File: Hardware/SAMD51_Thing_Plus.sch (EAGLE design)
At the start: 48 parts, among them J6 AMP FCI 10103594-0001LF, Q1 2.5A/30V, U1 MCP73831, U2 ATSAMD51J20A-A, U3 AP2112K-3.3V, U4 4MB Flash, Y1 32.768kHz

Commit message: Convert labels to Fredoka, headers to smaller square pads
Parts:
- J1: device SparkFun-Connectors:CONN_12NO_SILK -> SparkFun-Connectors:CONN_12SM_SQ_NO_SILK
- J2: device SparkFun-Connectors:CONN_161X16_NO_SILK -> SparkFun-Connectors:CONN_161X16_SM_SQ_NOSILK
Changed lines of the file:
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@@
 <part name="GND8" library="SparkFun-Aesthetics" deviceset="GND" device=""/>
 <part name="J6" library="SparkFun-Connectors" deviceset="USB_MICRO-B" device="_HALF_PTH" value="AMP FCI 10103594-0001LF"/>
-<part name="J1" library="SparkFun-Connectors" deviceset="CONN_12" device="NO_SILK"/>
-<part name="J2" library="SparkFun-Connectors" deviceset="CONN_16" device="1X16_NO_SILK"/>
+<part name="J1" library="SparkFun-Connectors" deviceset="CONN_12" device="SM_SQ_NO_SILK"/>
+<part name="J2" library="SparkFun-Connectors" deviceset="CONN_16" device="1X16_SM_SQ_NOSILK"/>
 <part name="GND5" library="SparkFun-Aesthetics" deviceset="GND" device=""/>
 <part name="GND7" library="SparkFun-Aesthetics" deviceset="GND" device=""/>

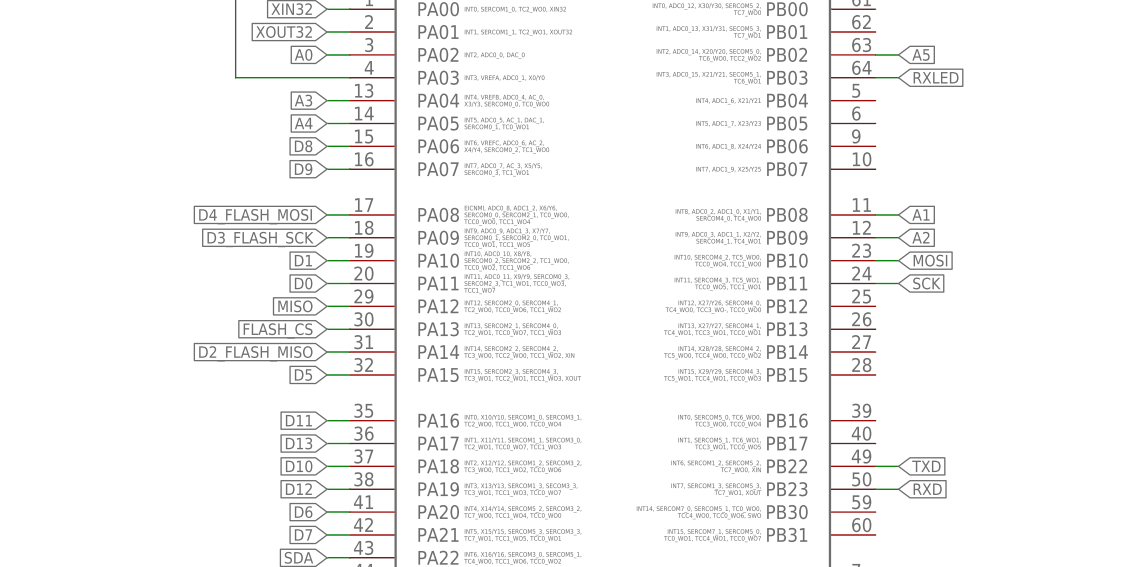
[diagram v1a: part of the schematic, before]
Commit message: Fix SPI pinout for flash and header
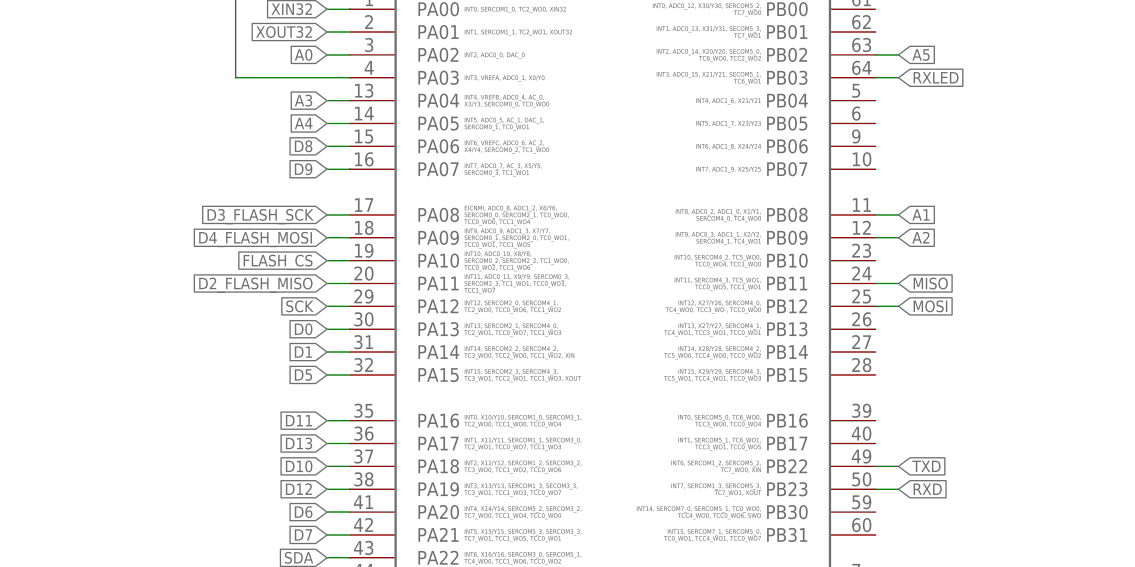
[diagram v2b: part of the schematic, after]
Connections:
- net D0: now also U2.PA13; no longer U2.PA11
- net D1: now also U2.PA14; no longer U2.PA10
- net D2_FLASH_MISO: now also U2.PA11; no longer U2.PA14
- net D3_FLASH_SCK: now also U2.PA08; no longer U2.PA09
- net D4_FLASH_MOSI: now also U2.PA09; no longer U2.PA08
- net FLASH_CS: now also U2.PA10; no longer U2.PA13
- net MISO: now also U2.PB11; no longer U2.PA12
- net MOSI: now also U2.PB12; no longer U2.PB10
- net SCK: now also U2.PA12; no longer U2.PB11
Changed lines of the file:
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@@
 <net name="D3_FLASH_SCK" class="0">
-<segment>
-<pinref part="U2" gate="G$1" pin="PA09"/>
-<wire x1="93.98" y1="121.92" x2="91.44" y2="121.92" width="0.1524" layer="91"/>
-<label x="91.44" y="121.92" size="1.27" layer="95" font="vector" rot="R180" xref="yes"/>
-</segment>
 <segment>
 <pinref part="U4" gate="G$1" pin="SCK"/>
@@
 <label x="396.24" y="152.4" size="1.27" layer="95" xref="yes"/>
 </segment>
+<segment>
+<pinref part="U2" gate="G$1" pin="PA08"/>
+<wire x1="93.98" y1="124.46" x2="91.44" y2="124.46" width="0.1524" layer="91"/>
+<label x="91.44" y="124.46" size="1.27" layer="95" rot="R180" xref="yes"/>
+</segment>
 </net>
 <net name="D2_FLASH_MISO" class="0">
-<segment>
-<pinref part="U2" gate="G$1" pin="PA14"/>
-<wire x1="93.98" y1="109.22" x2="91.44" y2="109.22" width="0.1524" layer="91"/>
-<label x="91.44" y="109.22" size="1.27" layer="95" font="vector" rot="R180" xref="yes"/>
-</segment>
 <segment>
 <pinref part="U4" gate="G$1" pin="SO(D1)"/>
 <wire x1="358.14" y1="154.94" x2="355.6" y2="154.94" width="0.1524" layer="91"/>
 <label x="355.6" y="154.94" size="1.27" layer="95" rot="R180" xref="yes"/>
+</segment>
+<segment>
+<pinref part="U2" gate="G$1" pin="PA11"/>
+<wire x1="93.98" y1="116.84" x2="91.44" y2="116.84" width="0.1524" layer="91"/>
+<label x="91.44" y="116.84" size="1.27" layer="95" rot="R180" xref="yes"/>
 </segment>
 </net>
@@
 <net name="D4_FLASH_MOSI" class="0">
 <segment>
-<pinref part="U2" gate="G$1" pin="PA08"/>
-<wire x1="93.98" y1="124.46" x2="91.44" y2="124.46" width="0.1524" layer="91"/>
-<label x="91.44" y="124.46" size="1.27" layer="95" font="vector" rot="R180" xref="yes"/>
-</segment>
-<segment>
 <pinref part="U4" gate="G$1" pin="SI(D0)"/>
 <wire x1="393.7" y1="149.86" x2="396.24" y2="149.86" width="0.1524" layer="91"/>
 <label x="396.24" y="149.86" size="1.27" layer="95" xref="yes"/>
+</segment>
+<segment>
+<pinref part="U2" gate="G$1" pin="PA09"/>
+<wire x1="93.98" y1="121.92" x2="91.44" y2="121.92" width="0.1524" layer="91"/>
+<label x="91.44" y="121.92" size="1.27" layer="95" rot="R180" xref="yes"/>
 </segment>
 </net>
@@
 </segment>
 <segment>
+<pinref part="U2" gate="G$1" pin="PA12"/>
+<wire x1="93.98" y1="114.3" x2="91.44" y2="114.3" width="0.1524" layer="91"/>
+<label x="91.44" y="114.3" size="1.27" layer="95" font="vector" rot="R180" xref="yes"/>
+</segment>
+</net>
+<net name="MOSI" class="0">
+<segment>
+<pinref part="J2" gate="G$1" pin="12"/>
+<wire x1="391.16" y1="66.04" x2="393.7" y2="66.04" width="0.1524" layer="91"/>
+<label x="393.7" y="66.04" size="1.27" layer="95" xref="yes"/>
+</segment>
+<segment>
+<pinref part="U2" gate="G$1" pin="PB12"/>
+<wire x1="152.4" y1="114.3" x2="154.94" y2="114.3" width="0.1524" layer="91"/>
+<label x="154.94" y="114.3" size="1.27" layer="95" xref="yes"/>
+</segment>
+</net>
+<net name="MISO" class="0">
+<segment>
+<pinref part="J2" gate="G$1" pin="13"/>
+<wire x1="391.16" y1="63.5" x2="393.7" y2="63.5" width="0.1524" layer="91"/>
+<label x="393.7" y="63.5" size="1.27" layer="95" xref="yes"/>
+</segment>
+<segment>
 <pinref part="U2" gate="G$1" pin="PB11"/>
 <wire x1="152.4" y1="116.84" x2="154.94" y2="116.84" width="0.1524" layer="91"/>
@@
 </segment>
 </net>
-<net name="MOSI" class="0">
-<segment>
-<pinref part="J2" gate="G$1" pin="12"/>
-<wire x1="391.16" y1="66.04" x2="393.7" y2="66.04" width="0.1524" layer="91"/>
-<label x="393.7" y="66.04" size="1.27" layer="95" xref="yes"/>
-</segment>
-<segment>
-<pinref part="U2" gate="G$1" pin="PB10"/>
-<wire x1="152.4" y1="119.38" x2="154.94" y2="119.38" width="0.1524" layer="91"/>
-<label x="154.94" y="119.38" size="1.27" layer="95" xref="yes"/>
-</segment>
-</net>
-<net name="MISO" class="0">
-<segment>
-<pinref part="J2" gate="G$1" pin="13"/>
-<wire x1="391.16" y1="63.5" x2="393.7" y2="63.5" width="0.1524" layer="91"/>
-<label x="393.7" y="63.5" size="1.27" layer="95" xref="yes"/>
-</segment>
-<segment>
-<pinref part="U2" gate="G$1" pin="PA12"/>
-<wire x1="93.98" y1="114.3" x2="91.44" y2="114.3" width="0.1524" layer="91"/>
-<label x="91.44" y="114.3" size="1.27" layer="95" font="vector" rot="R180" xref="yes"/>
-</segment>
-</net>
 <net name="D0" class="0">
 <segment>
@@
 </segment>
 <segment>
-<pinref part="U2" gate="G$1" pin="PA11"/>
-<wire x1="93.98" y1="116.84" x2="91.44" y2="116.84" width="0.1524" layer="91"/>
-<label x="91.44" y="116.84" size="1.27" layer="95" font="vector" rot="R180" xref="yes"/>
+<pinref part="U2" gate="G$1" pin="PA13"/>
+<wire x1="93.98" y1="111.76" x2="91.44" y2="111.76" width="0.1524" layer="91"/>
+<label x="91.44" y="111.76" size="1.27" layer="95" rot="R180" xref="yes"/>
 </segment>
 </net>
@@
 </segment>
 <segment>
-<pinref part="U2" gate="G$1" pin="PA10"/>
-<wire x1="93.98" y1="119.38" x2="91.44" y2="119.38" width="0.1524" layer="91"/>
-<label x="91.44" y="119.38" size="1.27" layer="95" font="vector" rot="R180" xref="yes"/>
+<pinref part="U2" gate="G$1" pin="PA14"/>
+<wire x1="93.98" y1="109.22" x2="91.44" y2="109.22" width="0.1524" layer="91"/>
+<label x="91.44" y="109.22" size="1.27" layer="95" rot="R180" xref="yes"/>
 </segment>
 </net>
@@
 </net>
 <net name="FLASH_CS" class="0">
-<segment>
-<pinref part="U2" gate="G$1" pin="PA13"/>
-<wire x1="93.98" y1="111.76" x2="91.44" y2="111.76" width="0.1524" layer="91"/>
-<label x="91.44" y="111.76" size="1.27" layer="95" rot="R180" xref="yes"/>
-</segment>
 <segment>
 <pinref part="U4" gate="G$1" pin="!CS"/>
@@
 <label x="350.52" y="157.48" size="1.016" layer="95"/>
 </segment>
-</net>
+<segment>
+<pinref part="U2" gate="G$1" pin="PA10"/>
+<wire x1="93.98" y1="119.38" x2="91.44" y2="119.38" width="0.1524" layer="91"/>
+<label x="91.44" y="119.38" size="1.27" layer="95" rot="R180" xref="yes"/>
+</segment>
+</net>

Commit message: updating version number
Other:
- note added: "02"
- note removed: "01"
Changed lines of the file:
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@@
 <?xml version="1.0" encoding="utf-8"?>
 <!DOCTYPE eagle SYSTEM "eagle.dtd">
-<eagle version="9.0.1">
+<eagle version="8.7.0">
 <drawing>
 <settings>
@@
 <text x="200.66" y="53.34" size="2.54" layer="94" font="vector" align="top-left">GPIO13 LED</text>
 <text x="332.74" y="104.14" size="2.54" layer="94" font="vector" align="top-left">Headers</text>
-<text x="421.64" y="10.16" size="2.54" layer="94" font="vector" align="top-left">01</text>
+<text x="421.64" y="10.16" size="2.54" layer="94" font="vector" align="top-left">02</text>
 <text x="69.088" y="17.78" size="0.4064" layer="94">C8 to be
 near U2.21</text>

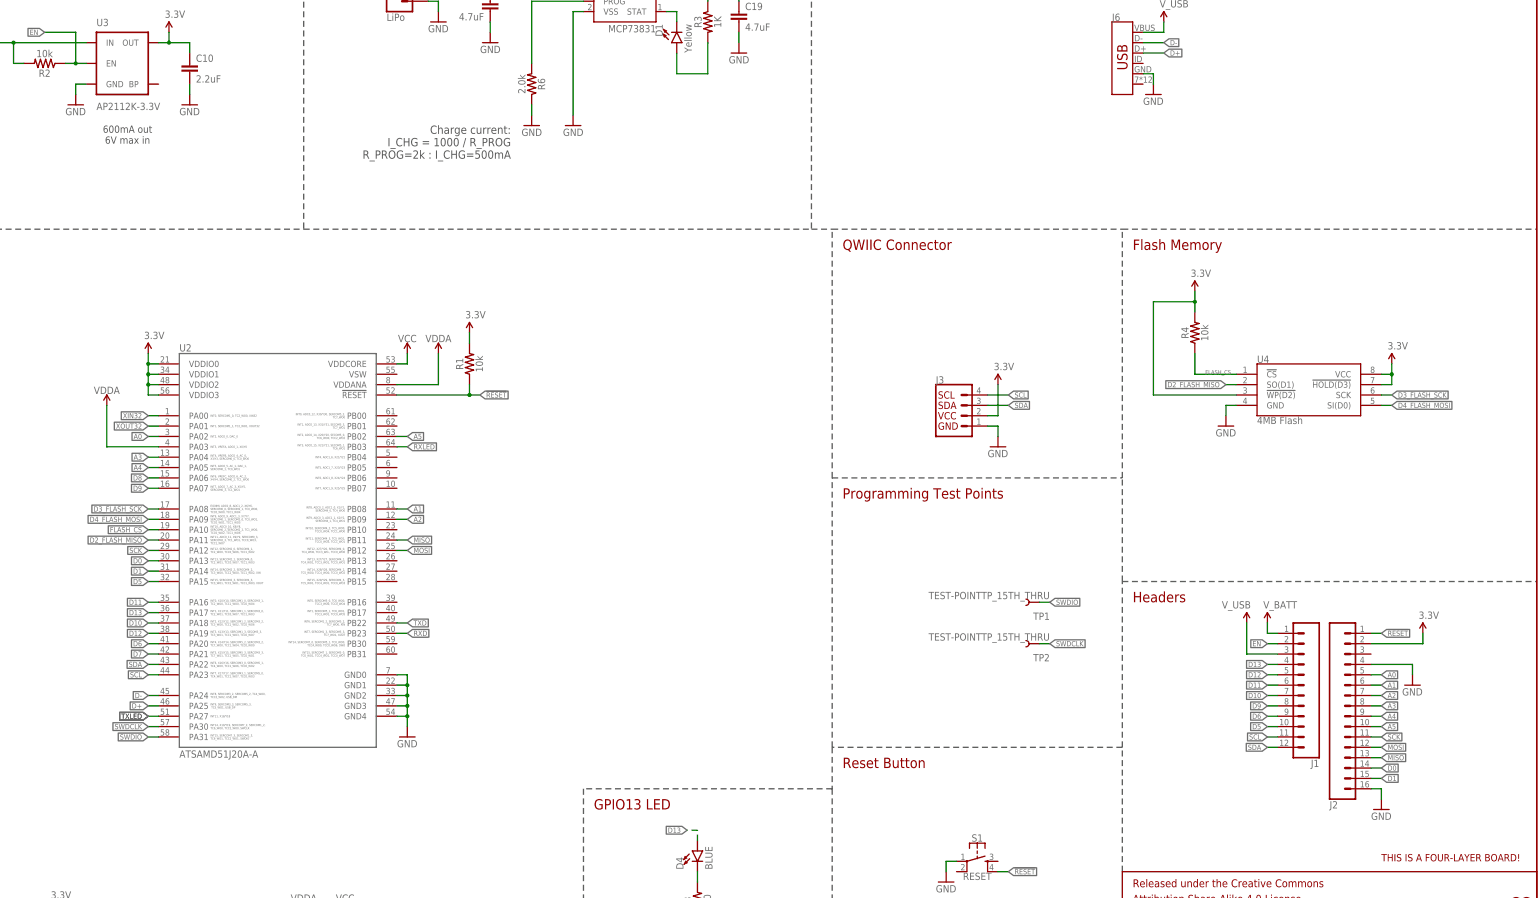
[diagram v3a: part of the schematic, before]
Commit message: connecting D4 to match feather footprint, removing short on USB connector
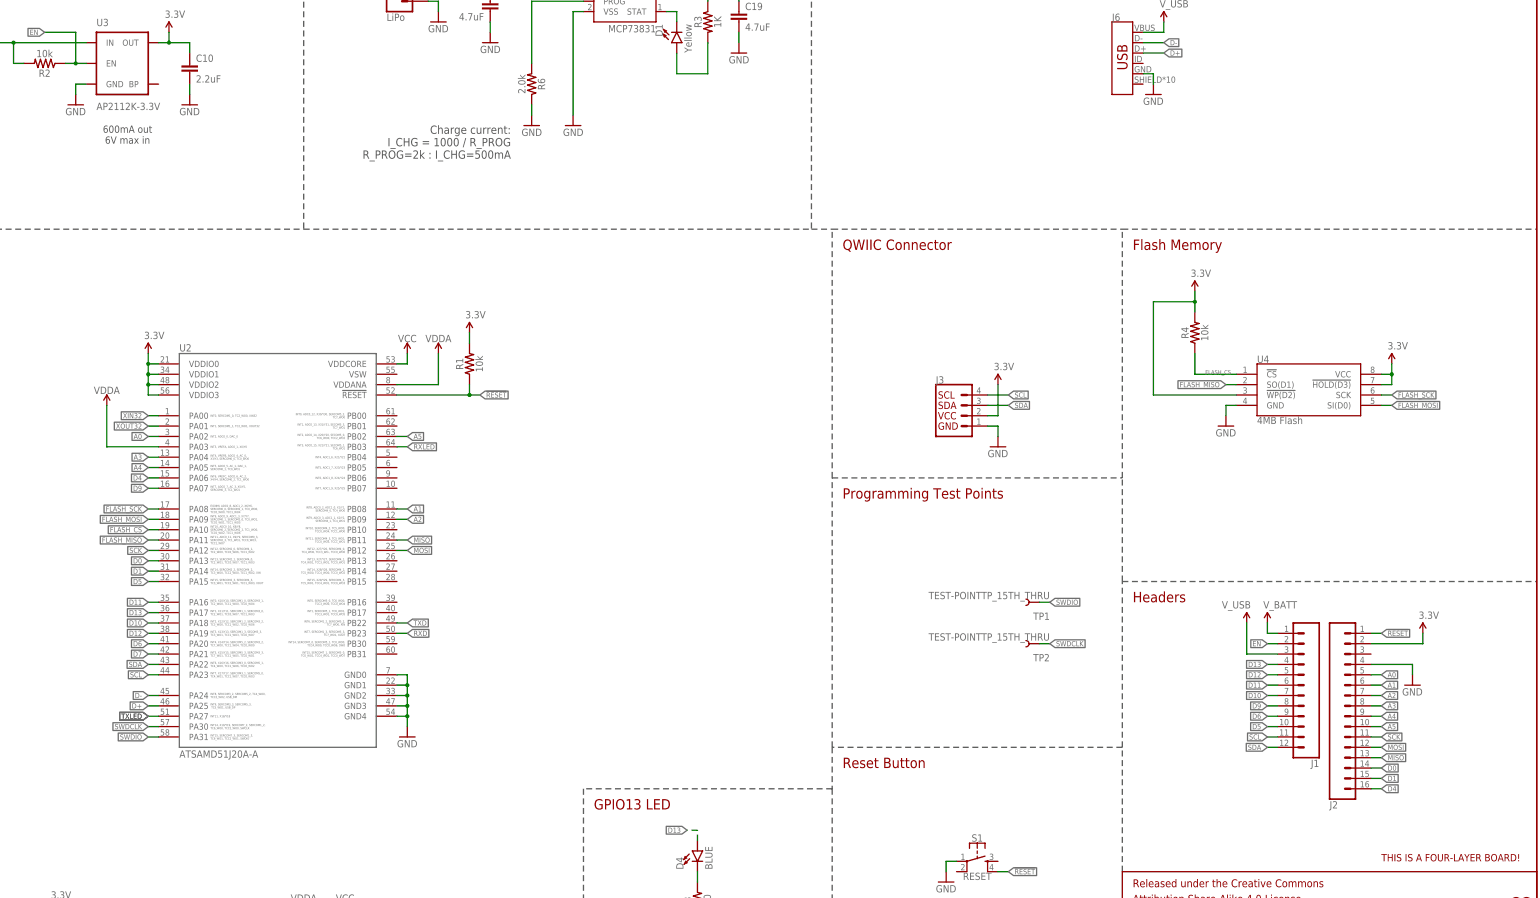
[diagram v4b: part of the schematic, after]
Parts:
- J6: device SparkFun-Connectors:USB_MICRO-B_HALF_PTH -> SparkFun-Connectors:USB_MICRO-B_HALF_PTH_MILL
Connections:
- net D2_FLASH_MISO renamed FLASH_MISO
- net D3_FLASH_SCK renamed FLASH_SCK
- net D4_FLASH_MOSI renamed FLASH_MOSI
- removed net D8: U2.PA06
- new net D4: J2.16, U2.PA06
- net GND: no longer J2.16
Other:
- moved on the sheet: J6
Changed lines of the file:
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@@
 <?xml version="1.0" encoding="utf-8"?>
 <!DOCTYPE eagle SYSTEM "eagle.dtd">
-<eagle version="8.7.0">
+<eagle version="9.1.0">
 <drawing>
 <settings>
@@
 <part name="SUPPLY10" library="SparkFun-Aesthetics" deviceset="3.3V" device=""/>
 <part name="GND8" library="SparkFun-Aesthetics" deviceset="GND" device=""/>
-<part name="J6" library="SparkFun-Connectors" deviceset="USB_MICRO-B" device="_HALF_PTH" value="AMP FCI 10103594-0001LF"/>
+<part name="J6" library="SparkFun-Connectors" deviceset="USB_MICRO-B" device="_HALF_PTH_MILL" value="AMP FCI 10103594-0001LF"/>
 <part name="J1" library="SparkFun-Connectors" deviceset="CONN_12" device="SM_SQ_NO_SILK"/>
 <part name="J2" library="SparkFun-Connectors" deviceset="CONN_16" device="1X16_SM_SQ_NOSILK"/>
-<part name="GND5" library="SparkFun-Aesthetics" deviceset="GND" device=""/>
 <part name="GND7" library="SparkFun-Aesthetics" deviceset="GND" device=""/>
 <part name="SUPPLY4" library="SparkFun-Aesthetics" deviceset="3.3V" device=""/>
@@
 <instance part="J1" gate="G$1" x="378.46" y="78.74" rot="R180"/>
 <instance part="J2" gate="G$1" x="381" y="73.66" rot="MR180"/>
-<instance part="GND5" gate="1" x="393.7" y="50.8"/>
 <instance part="GND7" gate="1" x="401.32" y="81.28"/>
 <instance part="SUPPLY4" gate="G$1" x="403.86" y="93.98"/>
@@
 </segment>
 <segment>
-<pinref part="J2" gate="G$1" pin="16"/>
-<wire x1="391.16" y1="55.88" x2="393.7" y2="55.88" width="0.1524" layer="91"/>
-<pinref part="GND5" gate="1" pin="GND"/>
-<wire x1="393.7" y1="53.34" x2="393.7" y2="55.88" width="0.1524" layer="91"/>
-</segment>
-<segment>
 <pinref part="J2" gate="G$1" pin="4"/>
 <wire x1="391.16" y1="86.36" x2="401.32" y2="86.36" width="0.1524" layer="91"/>
@@
 </segment>
 </net>
-<net name="D8" class="0">
+<net name="D4" class="0">
 <segment>
 <pinref part="U2" gate="G$1" pin="PA06"/>
@@
 <label x="91.44" y="132.08" size="1.27" layer="95" font="vector" rot="R180" xref="yes"/>
 </segment>
-</net>
-<net name="D3_FLASH_SCK" class="0">
+<segment>
+<pinref part="J2" gate="G$1" pin="16"/>
+<wire x1="391.16" y1="55.88" x2="393.7" y2="55.88" width="0.1524" layer="91"/>
+<label x="393.7" y="55.88" size="1.27" layer="95" xref="yes"/>
+</segment>
+</net>
+<net name="FLASH_SCK" class="0">
 <segment>
 <pinref part="U4" gate="G$1" pin="SCK"/>
@@
 <wire x1="93.98" y1="124.46" x2="91.44" y2="124.46" width="0.1524" layer="91"/>
 <label x="91.44" y="124.46" size="1.27" layer="95" rot="R180" xref="yes"/>
-</segment>
-</net>
-<net name="D2_FLASH_MISO" class="0">
-<segment>
-<pinref part="U4" gate="G$1" pin="SO(D1)"/>
-<wire x1="358.14" y1="154.94" x2="355.6" y2="154.94" width="0.1524" layer="91"/>
-<label x="355.6" y="154.94" size="1.27" layer="95" rot="R180" xref="yes"/>
-</segment>
-<segment>
-<pinref part="U2" gate="G$1" pin="PA11"/>
-<wire x1="93.98" y1="116.84" x2="91.44" y2="116.84" width="0.1524" layer="91"/>
-<label x="91.44" y="116.84" size="1.27" layer="95" rot="R180" xref="yes"/>
 </segment>
 </net>
@@
 </segment>
 </net>
-<net name="D4_FLASH_MOSI" class="0">
+<net name="FLASH_MOSI" class="0">
 <segment>
 <pinref part="U4" gate="G$1" pin="SI(D0)"/>
@@
 </segment>
 </net>
+<net name="FLASH_MISO" class="0">
+<segment>
+<pinref part="U2" gate="G$1" pin="PA11"/>
+<wire x1="93.98" y1="116.84" x2="91.44" y2="116.84" width="0.1524" layer="91"/>
+<label x="91.44" y="116.84" size="1.27" layer="95" rot="R180" xref="yes"/>
+</segment>
+<segment>
+<pinref part="U4" gate="G$1" pin="SO(D1)"/>
+<wire x1="358.14" y1="154.94" x2="355.6" y2="154.94" width="0.1524" layer="91"/>
+<label x="355.6" y="154.94" size="1.27" layer="95" rot="R180" xref="yes"/>
+</segment>
+</net>

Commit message: post checklist changes
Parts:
- removed JP2: LiPo, SparkFun-Connectors:CONN_02-JST-2MM-SMT
- added J4: (no value), SparkFun-Connectors:JST_2MM_MALE
- added JP1: JUMPER-SMT_3_2-NC_TRACE_SILK, SparkFun-Jumpers:JUMPER-SMT_3_2-NC_TRACE_SILK
- added R5, R9: 2.2k, SparkFun-Resistors:2.2KOHM-0603-1/10W-1%
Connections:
- new net N$2: JP1.3, R5.2
- new net N$3: JP1.1, R9.2
- net 3.3V: now also JP1.2
- net GND: now also J4.-; no longer JP2.1
- net SCL: now also R5.1
- net SDA: now also R9.1
- net V_BATT: now also J4.+; no longer JP2.2
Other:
- note added: "600mA out VIN: 2.5V-6V"
- note added: "M. Hord, M. West, A. England"
- note added: "v03"
- note removed: "02"
- note removed: "600mA out 6V max in"
- note removed: "Mike Hord"
- moved on the sheet: C10, C19, C6, C7, D1, D2, J3, J6, Q1, R2, R3, R4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
